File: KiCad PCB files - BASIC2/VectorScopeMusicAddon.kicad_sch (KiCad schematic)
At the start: 13 parts, among them J1 Conn_01x09_Socket, J3 AudioJack3_SwitchTR, SW1 SW_Push_DPDT, SW2 SW_Push_DPDT, U1 OPA2192

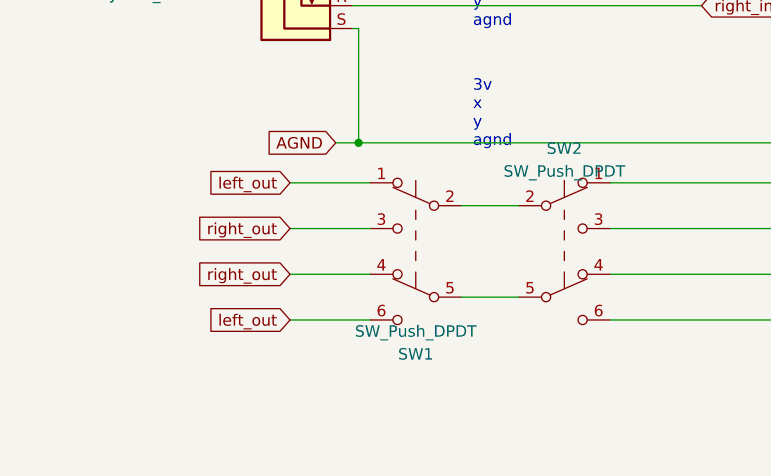
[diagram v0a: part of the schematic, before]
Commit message: added long version for Tina case
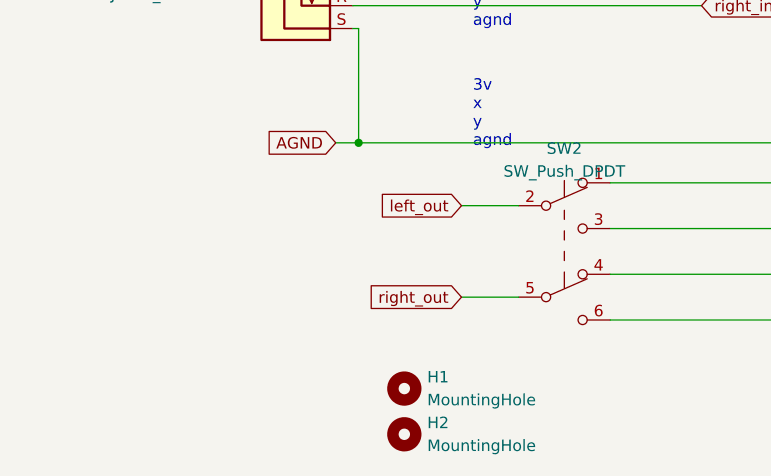
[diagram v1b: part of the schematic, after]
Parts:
- removed SW1: SW_Push_DPDT, Button_Switch_SMD:SW_DPDT_CK_JS202011JCQN, symbol Switch:SW_Push_DPDT
- added H1, H2: MountingHole, MountingHole:MountingHole_2.2mm_M2, symbol Mechanical:MountingHole
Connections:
- net left_out: now also SW2.2 (B)
- net right_out: now also SW2.5 (B)
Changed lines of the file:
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@@
-	(wire
-		(pts
-			(xy 53.34 92.71) (xy 44.45 92.71)
-		)
-		(stroke
-			(width 0)
-			(type default)
-		)
-	)
 	(wire
 		(pts
@@
 	(wire
 		(pts
-			(xy 53.34 97.79) (xy 44.45 97.79)
-		)
-		(stroke
-			(width 0)
-			(type default)
-		)
-	)
-	(wire
-		(pts
 			(xy 93.98 38.1) (xy 95.885 38.1)
 		)
@@
 	(wire
 		(pts
-			(xy 53.34 82.55) (xy 44.45 82.55)
-		)
-		(stroke
-			(width 0)
-			(type default)
-		)
-	)
-	(wire
-		(pts
 			(xy 51.435 65.405) (xy 52.07 65.405)
 		)
@@
 		(pts
 			(xy 63.5 85.09) (xy 69.85 85.09)
-		)
-		(stroke
-			(width 0)
-			(type default)
-		)
-	)
-	(wire
-		(pts
-			(xy 53.34 87.63) (xy 44.45 87.63)
 		)
 		(stroke
@@
 	(global_label "right_out"
 		(shape input)
-		(at 44.45 87.63 180)
+		(at 63.5 95.25 180)
 		(fields_autoplaced yes)
 		(effects
@@
 		)
 		(property "Intersheetrefs" "${INTERSHEET_REFS}"
-			(at 33.1382 87.63 0)
+			(at 52.1882 95.25 0)
 			(effects
 				(font
@@
 		)
 	)
-	(global_label "right_out"
+	(global_label "left_in"
 		(shape input)
-		(at 44.45 92.71 180)
+		(at 82.55 26.67 180)
 		(fields_autoplaced yes)
 		(effects
@@
 		)
 		(property "Intersheetrefs" "${INTERSHEET_REFS}"
-			(at 33.1382 92.71 0)
+			(at 73.7176 26.67 0)
 			(effects
 				(font
@@
 		)
 	)
-	(global_label "left_in"
+	(global_label "right_amp"
 		(shape input)
-		(at 82.55 26.67 180)
+		(at 99.06 97.79 0)
 		(fields_autoplaced yes)
 		(effects
@@
 				(size 1.27 1.27)
 			)
-			(justify right)
+			(justify left)
 		)
 		(property "Intersheetrefs" "${INTERSHEET_REFS}"
-			(at 73.7176 26.67 0)
-			(effects
-				(font
-					(size 1.27 1.27)
-				)
-				(justify right)
-				(hide yes)
-			)
-		)
-	)
-	(global_label "right_amp"
+			(at 111.3394 97.79 0)
+			(effects
+				(font
+					(size 1.27 1.27)
+				)
+				(justify left)
+				(hide yes)
+			)
+		)
+	)
+	(global_label "right_in"
 		(shape input)
-		(at 99.06 97.79 0)
+		(at 90.17 62.865 0)
 		(fields_autoplaced yes)
 		(effects
@@
 		)
 		(property "Intersheetrefs" "${INTERSHEET_REFS}"
-			(at 111.3394 97.79 0)
+			(at 100.2119 62.865 0)
 			(effects
 				(font
@@
 		)
 	)
-	(global_label "right_in"
+	(global_label "right_out"
 		(shape input)
-		(at 90.17 62.865 0)
+		(at 126.365 62.865 180)
 		(fields_autoplaced yes)
 		(effects
@@
 				(size 1.27 1.27)
 			)
-			(justify left)
+			(justify right)
 		)
 		(property "Intersheetrefs" "${INTERSHEET_REFS}"
-			(at 100.2119 62.865 0)
-			(effects
-				(font
-					(size 1.27 1.27)
-				)
-				(justify left)
-				(hide yes)
-			)
-		)
-	)
-	(global_label "right_out"
+			(at 115.0532 62.865 0)
+			(effects
+				(font
+					(size 1.27 1.27)
+				)
+				(justify right)
+				(hide yes)
+			)
+		)
+	)
+	(global_label "left_out"
 		(shape input)
-		(at 126.365 62.865 180)
+		(at 126.365 60.325 180)
 		(fields_autoplaced yes)
 		(effects
@@
 		)
 		(property "Intersheetrefs" "${INTERSHEET_REFS}"
-			(at 115.0532 62.865 0)
+			(at 116.2627 60.325 0)
 			(effects
 				(font
@@
 	(global_label "left_out"
 		(shape input)
-		(at 126.365 60.325 180)
+		(at 63.5 85.09 180)
 		(fields_autoplaced yes)
 		(effects
@@
 		)
 		(property "Intersheetrefs" "${INTERSHEET_REFS}"
-			(at 116.2627 60.325 0)
+			(at 53.3977 85.09 0)
 			(effects
 				(font
@@
 		)
 	)
-	(global_label "left_out"
+	(global_label "left_amp"
 		(shape input)
-		(at 44.45 82.55 180)
+		(at 116.205 35.56 0)
 		(fields_autoplaced yes)
 		(effects
@@
 				(size 1.27 1.27)
 			)
-			(justify right)
-		)
-		(property "Intersheetrefs" "${INTERSHEET_REFS}"
-			(at 34.3477 82.55 0)
-			(effects
-				(font
-					(size 1.27 1.27)
-				)
-				(justify right)
-				(hide yes)
-			)
-		)
-	)
-	(global_label "left_out"
-		(shape input)
-		(at 44.45 97.79 180)
-		(fields_autoplaced yes)
-		(effects
-			(font
-				(size 1.27 1.27)
-			)
-			(justify right)
-		)
-		(property "Intersheetrefs" "${INTERSHEET_REFS}"
-			(at 34.3477 97.79 0)
-			(effects
-				(font
-					(size 1.27 1.27)
-				)
-				(justify right)
-				(hide yes)
-			)
-		)
-	)
-	(global_label "left_amp"
-		(shape input)
-		(at 116.205 35.56 0)
-		(fields_autoplaced yes)
-		(effects
-			(font
-				(size 1.27 1.27)
-			)
 			(justify left)
 		)
@@
 				(justify left)
 				(hide yes)
+			)
+		)
+	)
+	(symbol
+		(lib_id "Mechanical:MountingHole")
+		(at 57.15 105.41 0)
+		(unit 1)
+		(exclude_from_sim yes)
+		(in_bom no)
+		(on_board yes)
+		(dnp no)
+		(fields_autoplaced yes)
+		(property "Reference" "H1"
+			(at 59.69 104.1399 0)
+			(effects
+				(font
+					(size 1.27 1.27)
+				)
+				(justify left)
+			)
+		)
+		(property "Value" "MountingHole"
+			(at 59.69 106.6799 0)
+			(effects
+				(font
+					(size 1.27 1.27)
+				)
+				(justify left)
+			)
+		)
+		(property "Footprint" "MountingHole:MountingHole_2.2mm_M2"
+			(at 57.15 105.41 0)
+			(effects
+				(font
+					(size 1.27 1.27)
+				)
+				(hide yes)
+			)
+		)
+		(property "Datasheet" "~"
+			(at 57.15 105.41 0)
+			(effects
+				(font
+					(size 1.27 1.27)
+				)
+				(hide yes)
+			)
+		)
+		(property "Description" "Mounting Hole without connection"
+			(at 57.15 105.41 0)
+			(effects
+				(font
+					(size 1.27 1.27)
+				)
+				(hide yes)
+			)
+		)
+		(instances
+			(project ""
+				(path "/af256697-7c61-4a78-86ce-ea788b0b3065"
+					(reference "H1")
+					(unit 1)
+				)
 			)
 		)
@@
 	)
 	(symbol
-		(lib_id "Switch:SW_Push_DPDT")
-		(at 58.42 90.17 0)
-		(mirror y)
-		(unit 1)
-		(exclude_from_sim no)
-		(in_bom yes)
-		(on_board yes)
-		(dnp no)
-		(property "Reference" "SW1"
-			(at 58.42 101.6 0)
-			(effects
-				(font
-					(size 1.27 1.27)
-				)
-			)
-		)
-		(property "Value" "SW_Push_DPDT"
-			(at 58.42 99.06 0)
-			(effects
-				(font
-					(size 1.27 1.27)
-				)
-			)
-		)
-		(property "Footprint" "Button_Switch_SMD:SW_DPDT_CK_JS202011JCQN"
-			(at 58.42 85.09 0)
-			(effects
-				(font
-					(size 1.27 1.27)
-				)
-				(hide yes)
-			)
-		)
-		(property "Datasheet" "~"
-			(at 58.42 85.09 0)
-			(effects
-				(font
-					(size 1.27 1.27)
-				)
-				(hide yes)
-			)
-		)
-		(property "Description" ""
-			(at 58.42 90.17 0)
-			(effects
-				(font
-					(size 1.27 1.27)
-				)
-				(hide yes)
-			)
-		)
-		(property "MPN" "C221665"
-			(at 58.42 90.17 0)
-			(effects
-				(font
-					(size 1.27 1.27)
-				)
-				(hide yes)
-			)
-		)
-		(pin "1"
-		)
-		(pin "2"
-		)
-		(pin "3"
-		)
-		(pin "4"
-		)
-		(pin "5"
-		)
-		(pin "6"
-		)
-		(instances
-			(project "VectorScopeMusicAddon"
-				(path "/af256697-7c61-4a78-86ce-ea788b0b3065"
-					(reference "SW1")
-					(unit 1)
-				)
-			)
-		)
-	)
-	(symbol
 		(lib_id "power:VCC")
 		(at 82.55 33.02 90)
@@
 					(unit 1)
 				)
+			)
+		)
+	)
+	(symbol
+		(lib_id "Mechanical:MountingHole")
+		(at 57.15 110.49 0)
+		(unit 1)
+		(exclude_from_sim yes)
+		(in_bom no)
+		(on_board yes)
+		(dnp no)
+		(fields_autoplaced yes)
+		(property "Reference" "H2"
+			(at 59.69 109.2199 0)
+			(effects
+				(font
+					(size 1.27 1.27)
+				)
+				(justify left)
+			)
+		)
+		(property "Value" "MountingHole"
+			(at 59.69 111.7599 0)
+			(effects
+				(font
+					(size 1.27 1.27)
+				)
+				(justify left)
+			)
+		)
+		(property "Footprint" "MountingHole:MountingHole_2.2mm_M2"
+			(at 57.15 110.49 0)
+			(effects
+				(font
+					(size 1.27 1.27)
+				)
+				(hide yes)
+			)
+		)
+		(property "Datasheet" "~"
+			(at 57.15 110.49 0)
+			(effects
+				(font
+					(size 1.27 1.27)
+				)
+				(hide yes)
+			)
+		)
+		(property "Description" "Mounting Hole without connection"
+			(at 57.15 110.49 0)
+			(effects
+				(font
+					(size 1.27 1.27)
+				)
+				(hide yes)
+			)
+		)
+		(instances
+			(project "VectorScopeMusicAddon"
+				(path "/af256697-7c61-4a78-86ce-ea788b0b3065"
+					(reference "H2")
+					(unit 1)
+				)
